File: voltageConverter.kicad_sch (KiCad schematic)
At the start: 5 parts, among them IC1 Voltage Converter (ADP7158ARD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

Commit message: Finished schematic and fully routed PCB.
Signed-off-by: Logan Tolbert <xem6df@virginia.edu>
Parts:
- renumbered C5 to C12, C6 to C13, C7 to C14, C8 to C15
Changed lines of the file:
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@@
 		(dnp no)
 		(fields_autoplaced yes)
-		(property "Reference" "C6"
+		(property "Reference" "C13"
 			(at 121.92 87.6299 0)
 			(effects
@@
 			(project "COMM"
 				(path "/b0bd204d-ca77-4624-acd2-31813bf00a6c/aa984c0d-c4b1-428c-b5e1-c08f8c2d2b92"
-					(reference "C6")
+					(reference "C13")
 					(unit 1)
 				)
@@
 		(dnp no)
 		(fields_autoplaced yes)
-		(property "Reference" "C8"
+		(property "Reference" "C15"
 			(at 190.5 82.5499 0)
 			(effects
@@
 			(project "COMM"
 				(path "/b0bd204d-ca77-4624-acd2-31813bf00a6c/aa984c0d-c4b1-428c-b5e1-c08f8c2d2b92"
-					(reference "C8")
+					(reference "C15")
 					(unit 1)
 				)
@@
 		(dnp no)
 		(fields_autoplaced yes)
-		(property "Reference" "#PWR023"
+		(property "Reference" "#PWR030"
 			(at 152.4 107.95 0)
 			(effects
@@
 			(project "COMM"
 				(path "/b0bd204d-ca77-4624-acd2-31813bf00a6c/aa984c0d-c4b1-428c-b5e1-c08f8c2d2b92"
-					(reference "#PWR023")
+					(reference "#PWR030")
 					(unit 1)
 				)
@@
 		(dnp no)
 		(fields_autoplaced yes)
-		(property "Reference" "#PWR024"
+		(property "Reference" "#PWR031"
 			(at 180.34 107.95 0)
 			(effects
@@
 			(project "COMM"
 				(path "/b0bd204d-ca77-4624-acd2-31813bf00a6c/aa984c0d-c4b1-428c-b5e1-c08f8c2d2b92"
-					(reference "#PWR024")
+					(reference "#PWR031")
 					(unit 1)
 				)
@@
 		(dnp no)
 		(fields_autoplaced yes)
-		(property "Reference" "#PWR025"
+		(property "Reference" "#PWR032"
 			(at 186.69 93.98 0)
 			(effects
@@
 			(project "COMM"
 				(path "/b0bd204d-ca77-4624-acd2-31813bf00a6c/aa984c0d-c4b1-428c-b5e1-c08f8c2d2b92"
-					(reference "#PWR025")
+					(reference "#PWR032")
 					(unit 1)
 				)
@@
 		(dnp no)
 		(fields_autoplaced yes)
-		(property "Reference" "C7"
+		(property "Reference" "C14"
 			(at 184.15 96.5199 0)
 			(effects
@@
 			(project "COMM"
 				(path "/b0bd204d-ca77-4624-acd2-31813bf00a6c/aa984c0d-c4b1-428c-b5e1-c08f8c2d2b92"
-					(reference "C7")
+					(reference "C14")
 					(unit 1)
 				)
@@
 		(dnp no)
 		(fields_autoplaced yes)
-		(property "Reference" "C5"
+		(property "Reference" "C12"
 			(at 107.95 87.6299 0)
 			(effects
@@
 			(project "COMM"
 				(path "/b0bd204d-ca77-4624-acd2-31813bf00a6c/aa984c0d-c4b1-428c-b5e1-c08f8c2d2b92"
-					(reference "C5")
+					(reference "C12")
 					(unit 1)
 				)
@@
 		(dnp no)
 		(fields_autoplaced yes)
-		(property "Reference" "#PWR022"
+		(property "Reference" "#PWR029"
 			(at 118.11 99.06 0)
 			(effects
@@
 			(project "COMM"
 				(path "/b0bd204d-ca77-4624-acd2-31813bf00a6c/aa984c0d-c4b1-428c-b5e1-c08f8c2d2b92"
-					(reference "#PWR022")
+					(reference "#PWR029")
 					(unit 1)
 				)
@@
 		(dnp no)
 		(fields_autoplaced yes)
-		(property "Reference" "#PWR021"
+		(property "Reference" "#PWR028"
 			(at 104.14 99.06 0)
 			(effects
@@
 			(project "COMM"
 				(path "/b0bd204d-ca77-4624-acd2-31813bf00a6c/aa984c0d-c4b1-428c-b5e1-c08f8c2d2b92"
-					(reference "#PWR021")
-					(unit 1)
-				)
+					(reference "#PWR028")
+					(unit 1)
+				)

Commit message: Added pull-up to CS pin on DMR module.
Signed-off-by: Logan Tolbert <xem6df@virginia.edu>
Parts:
- renumbered C12 to C11, C13 to C12, C14 to C13, C15 to C14
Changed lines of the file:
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@@
 		(dnp no)
 		(fields_autoplaced yes)
-		(property "Reference" "C13"
+		(property "Reference" "C12"
 			(at 121.92 87.6299 0)
 			(effects
@@
 			(project "COMM"
 				(path "/b0bd204d-ca77-4624-acd2-31813bf00a6c/aa984c0d-c4b1-428c-b5e1-c08f8c2d2b92"
-					(reference "C13")
+					(reference "C12")
 					(unit 1)
 				)
@@
 		(dnp no)
 		(fields_autoplaced yes)
-		(property "Reference" "C15"
+		(property "Reference" "C14"
 			(at 190.5 82.5499 0)
 			(effects
@@
 			(project "COMM"
 				(path "/b0bd204d-ca77-4624-acd2-31813bf00a6c/aa984c0d-c4b1-428c-b5e1-c08f8c2d2b92"
-					(reference "C15")
+					(reference "C14")
 					(unit 1)
 				)
@@
 		(dnp no)
 		(fields_autoplaced yes)
-		(property "Reference" "#PWR030"
+		(property "Reference" "#PWR029"
 			(at 152.4 107.95 0)
 			(effects
@@
 			(project "COMM"
 				(path "/b0bd204d-ca77-4624-acd2-31813bf00a6c/aa984c0d-c4b1-428c-b5e1-c08f8c2d2b92"
-					(reference "#PWR030")
+					(reference "#PWR029")
 					(unit 1)
 				)
@@
 		(dnp no)
 		(fields_autoplaced yes)
-		(property "Reference" "#PWR031"
+		(property "Reference" "#PWR030"
 			(at 180.34 107.95 0)
 			(effects
@@
 			(project "COMM"
 				(path "/b0bd204d-ca77-4624-acd2-31813bf00a6c/aa984c0d-c4b1-428c-b5e1-c08f8c2d2b92"
-					(reference "#PWR031")
+					(reference "#PWR030")
 					(unit 1)
 				)
@@
 		(dnp no)
 		(fields_autoplaced yes)
-		(property "Reference" "#PWR032"
+		(property "Reference" "#PWR031"
 			(at 186.69 93.98 0)
 			(effects
@@
 			(project "COMM"
 				(path "/b0bd204d-ca77-4624-acd2-31813bf00a6c/aa984c0d-c4b1-428c-b5e1-c08f8c2d2b92"
-					(reference "#PWR032")
+					(reference "#PWR031")
 					(unit 1)
 				)
@@
 		(dnp no)
 		(fields_autoplaced yes)
-		(property "Reference" "C14"
+		(property "Reference" "C13"
 			(at 184.15 96.5199 0)
 			(effects
@@
 			(project "COMM"
 				(path "/b0bd204d-ca77-4624-acd2-31813bf00a6c/aa984c0d-c4b1-428c-b5e1-c08f8c2d2b92"
-					(reference "C14")
+					(reference "C13")
 					(unit 1)
 				)
@@
 		(dnp no)
 		(fields_autoplaced yes)
-		(property "Reference" "C12"
+		(property "Reference" "C11"
 			(at 107.95 87.6299 0)
 			(effects
@@
 			(project "COMM"
 				(path "/b0bd204d-ca77-4624-acd2-31813bf00a6c/aa984c0d-c4b1-428c-b5e1-c08f8c2d2b92"
-					(reference "C12")
+					(reference "C11")
 					(unit 1)
 				)
@@
 		(dnp no)
 		(fields_autoplaced yes)
-		(property "Reference" "#PWR029"
+		(property "Reference" "#PWR028"
 			(at 118.11 99.06 0)
 			(effects
@@
 			(project "COMM"
 				(path "/b0bd204d-ca77-4624-acd2-31813bf00a6c/aa984c0d-c4b1-428c-b5e1-c08f8c2d2b92"
-					(reference "#PWR029")
+					(reference "#PWR028")
 					(unit 1)
 				)
@@
 		(dnp no)
 		(fields_autoplaced yes)
-		(property "Reference" "#PWR028"
+		(property "Reference" "#PWR027"
 			(at 104.14 99.06 0)
 			(effects
@@
 			(project "COMM"
 				(path "/b0bd204d-ca77-4624-acd2-31813bf00a6c/aa984c0d-c4b1-428c-b5e1-c08f8c2d2b92"
-					(reference "#PWR028")
-					(unit 1)
-				)
+					(reference "#PWR027")
+					(unit 1)
+				)

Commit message: Addressed most comments from McPherson, modified schematic.
Signed-off-by: Logan Tolbert <xem6df@virginia.edu>
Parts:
- added C21: 10 μF, C_10uF:CAPC1005X70N, symbol Device:C
- renumbered C11 to C17, C12 to C18, C13 to C19, C14 to C20
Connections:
- net GND: now also C21.2
- net VIN: now also C21.1
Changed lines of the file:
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@@
+	)
+	(junction
+		(at 196.85 109.22)
+		(diameter 0)
+		(color 0 0 0 0)
 	)
 	(junction
@@
 		(pts
 			(xy 180.34 85.09) (xy 180.34 93.98)
+		)
+		(stroke
+			(width 0)
+			(type default)
+		)
+	)
+	(wire
+		(pts
+			(xy 196.85 110.49) (xy 196.85 109.22)
 		)
 		(stroke
@@
 		(dnp no)
 		(fields_autoplaced yes)
-		(property "Reference" "C12"
+		(property "Reference" "C18"
 			(at 121.92 87.6299 0)
 			(effects
@@
 			(project "COMM"
 				(path "/b0bd204d-ca77-4624-acd2-31813bf00a6c/aa984c0d-c4b1-428c-b5e1-c08f8c2d2b92"
-					(reference "C12")
+					(reference "C18")
 					(unit 1)
 				)
@@
 		(dnp no)
 		(fields_autoplaced yes)
-		(property "Reference" "C14"
+		(property "Reference" "C20"
 			(at 190.5 82.5499 0)
 			(effects
@@
 			(project "COMM"
 				(path "/b0bd204d-ca77-4624-acd2-31813bf00a6c/aa984c0d-c4b1-428c-b5e1-c08f8c2d2b92"
-					(reference "C14")
+					(reference "C20")
 					(unit 1)
 				)
@@
 		(dnp no)
 		(fields_autoplaced yes)
-		(property "Reference" "#PWR029"
+		(property "Reference" "#PWR041"
 			(at 152.4 107.95 0)
 			(effects
@@
 			(project "COMM"
 				(path "/b0bd204d-ca77-4624-acd2-31813bf00a6c/aa984c0d-c4b1-428c-b5e1-c08f8c2d2b92"
-					(reference "#PWR029")
+					(reference "#PWR041")
 					(unit 1)
 				)
@@
 		(dnp no)
 		(fields_autoplaced yes)
-		(property "Reference" "#PWR030"
+		(property "Reference" "#PWR042"
 			(at 180.34 107.95 0)
 			(effects
@@
 			(project "COMM"
 				(path "/b0bd204d-ca77-4624-acd2-31813bf00a6c/aa984c0d-c4b1-428c-b5e1-c08f8c2d2b92"
-					(reference "#PWR030")
+					(reference "#PWR042")
 					(unit 1)
 				)
@@
 		(dnp no)
 		(fields_autoplaced yes)
-		(property "Reference" "#PWR031"
+		(property "Reference" "#PWR043"
 			(at 186.69 93.98 0)
 			(effects
@@
 			(project "COMM"
 				(path "/b0bd204d-ca77-4624-acd2-31813bf00a6c/aa984c0d-c4b1-428c-b5e1-c08f8c2d2b92"
-					(reference "#PWR031")
+					(reference "#PWR043")
 					(unit 1)
 				)
@@
 		(dnp no)
 		(fields_autoplaced yes)
-		(property "Reference" "C13"
+		(property "Reference" "C19"
 			(at 184.15 96.5199 0)
 			(effects
@@
 			(project "COMM"
 				(path "/b0bd204d-ca77-4624-acd2-31813bf00a6c/aa984c0d-c4b1-428c-b5e1-c08f8c2d2b92"
-					(reference "C13")
+					(reference "C19")
 					(unit 1)
 				)
@@
 		(dnp no)
 		(fields_autoplaced yes)
-		(property "Reference" "C11"
+		(property "Reference" "C17"
 			(at 107.95 87.6299 0)
 			(effects
@@
 			(project "COMM"
 				(path "/b0bd204d-ca77-4624-acd2-31813bf00a6c/aa984c0d-c4b1-428c-b5e1-c08f8c2d2b92"
-					(reference "C11")
+					(reference "C17")
 					(unit 1)
 				)
@@
 	(symbol
 		(lib_id "power:GND")
+		(at 196.85 118.11 0)
+		(unit 1)
+		(exclude_from_sim no)
+		(in_bom yes)
+		(on_board yes)
+		(dnp no)
+		(fields_autoplaced yes)
+		(property "Reference" "#PWR044"
+			(at 196.85 124.46 0)
+			(effects
+				(font
+					(size 1.27 1.27)
+				)
+				(hide yes)
+			)
+		)
+		(property "Value" "GND"
+			(at 196.85 123.19 0)
+			(effects
+				(font
+					(size 1.27 1.27)
+				)
+			)
+		)
+		(property "Footprint" ""
+			(at 196.85 118.11 0)
+			(effects
+				(font
+					(size 1.27 1.27)
+				)
+				(hide yes)
+			)
+		)
+		(property "Datasheet" ""
+			(at 196.85 118.11 0)
+			(effects
+				(font
+					(size 1.27 1.27)
+				)
+				(hide yes)
+			)
+		)
+		(property "Description" "Power symbol creates a global label with name \"GND\" , ground"
+			(at 196.85 118.11 0)
+			(effects
+				(font
+					(size 1.27 1.27)
+				)
+				(hide yes)
+			)
+		)
+		(pin "1"
+		)
+		(instances
+			(project "COMM"
+				(path "/b0bd204d-ca77-4624-acd2-31813bf00a6c/aa984c0d-c4b1-428c-b5e1-c08f8c2d2b92"
+					(reference "#PWR044")
+					(unit 1)
+				)
+			)
+		)
+	)
+	(symbol
+		(lib_id "Device:C")
+		(at 196.85 114.3 0)
+		(unit 1)
+		(exclude_from_sim no)
+		(in_bom yes)
+		(on_board yes)
+		(dnp no)
+		(fields_autoplaced yes)
+		(property "Reference" "C21"
+			(at 200.66 113.0299 0)
+			(effects
+				(font
+					(size 1.27 1.27)
+				)
+				(justify left)
+			)
+		)
+		(property "Value" "10 μF"
+			(at 200.66 115.5699 0)
+			(effects
+				(font
+					(size 1.27 1.27)
+				)
+				(justify left)
+			)
+		)
+		(property "Footprint" "C_10uF:CAPC1005X70N"
+			(at 197.8152 118.11 0)
+			(effects
+				(font
+					(size 1.27 1.27)
+				)
+				(hide yes)
+			)
+		)
+		(property "Datasheet" "~"
+			(at 196.85 114.3 0)
+			(effects
+				(font
+					(size 1.27 1.27)
+				)
+				(hide yes)
+			)
+		)
+		(property "Description" "Unpolarized capacitor"
+			(at 196.85 114.3 0)
+			(effects
+				(font
+					(size 1.27 1.27)
+				)
+				(hide yes)
+			)
+		)
+		(pin "2"
+		)
+		(pin "1"
+		)
+		(instances
+			(project "COMM"
+				(path "/b0bd204d-ca77-4624-acd2-31813bf00a6c/aa984c0d-c4b1-428c-b5e1-c08f8c2d2b92"
+					(reference "C21")
+					(unit 1)
+				)
+			)
+		)
+	)
+	(symbol
+		(lib_id "power:GND")
 		(at 118.11 92.71 0)
 		(unit 1)
@@
 		(dnp no)
 		(fields_autoplaced yes)
-		(property "Reference" "#PWR028"
+		(property "Reference" "#PWR040"
 			(at 118.11 99.06 0)
 			(effects
@@
 			(project "COMM"
 				(path "/b0bd204d-ca77-4624-acd2-31813bf00a6c/aa984c0d-c4b1-428c-b5e1-c08f8c2d2b92"
-					(reference "#PWR028")
+					(reference "#PWR040")
 					(unit 1)
 				)
@@
 		(dnp no)
 		(fields_autoplaced yes)
-		(property "Reference" "#PWR027"
+		(property "Reference" "#PWR039"
 			(at 104.14 99.06 0)
 			(effects
@@
 			(project "COMM"
 				(path "/b0bd204d-ca77-4624-acd2-31813bf00a6c/aa984c0d-c4b1-428c-b5e1-c08f8c2d2b92"
-					(reference "#PWR027")
+					(reference "#PWR039")
 					(unit 1)
 				)

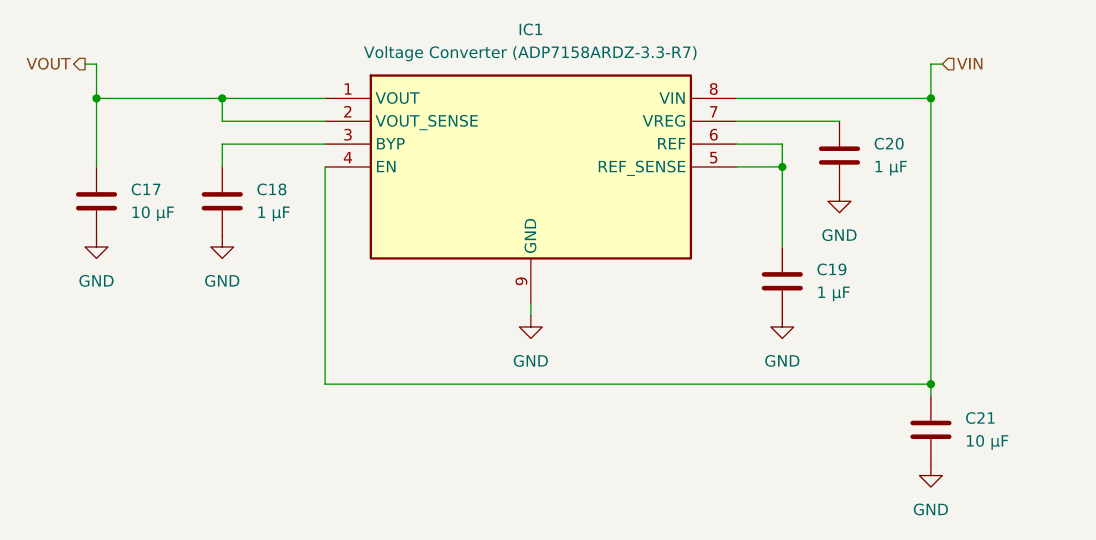
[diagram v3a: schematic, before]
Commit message: Finalized board design, updated DMR module to DMR818S-5W exact dimensions, rerouted PCB according to McPherson's comments. Added TLV61047 5V to 8V booster module.
Signed-off-by: Logan Tolbert <xem6df@virginia.edu>
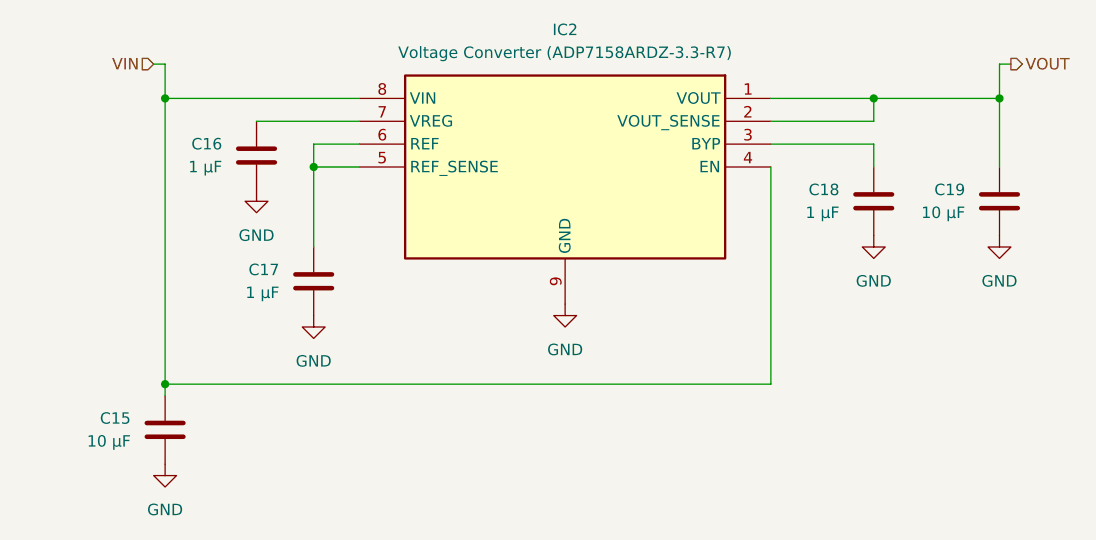
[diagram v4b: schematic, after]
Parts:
- renumbered C21 to C15, C20 to C16, C19 to C17, C17 to C19, IC1 to IC2
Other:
- moved on the sheet: C15, C16, C17, C18, C19, IC2

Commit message: Final COMM board design as of Feb 12 2026, ready to order.
Signed-off-by: Logan Tolbert <xem6df@virginia.edu>
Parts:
- renumbered C15 to C12, C16 to C13, C17 to C14, C18 to C15, C19 to C16
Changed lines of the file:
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@@
 		(dnp no)
 		(fields_autoplaced yes)
-		(property "Reference" "C18"
+		(property "Reference" "C15"
 			(at 186.69 87.6299 0)
 			(effects
@@
 			(project "COMM"
 				(path "/b0bd204d-ca77-4624-acd2-31813bf00a6c/aa984c0d-c4b1-428c-b5e1-c08f8c2d2b92"
-					(reference "C18")
+					(reference "C15")
 					(unit 1)
 				)
@@
 		(dnp no)
 		(fields_autoplaced yes)
-		(property "Reference" "C16"
+		(property "Reference" "C13"
 			(at 118.11 82.5499 0)
 			(effects
@@
 			(project "COMM"
 				(path "/b0bd204d-ca77-4624-acd2-31813bf00a6c/aa984c0d-c4b1-428c-b5e1-c08f8c2d2b92"
-					(reference "C16")
+					(reference "C13")
 					(unit 1)
 				)
@@
 		(dnp no)
 		(fields_autoplaced yes)
-		(property "Reference" "#PWR040"
+		(property "Reference" "#PWR038"
 			(at 156.21 106.68 0)
 			(effects
@@
 			(project "COMM"
 				(path "/b0bd204d-ca77-4624-acd2-31813bf00a6c/aa984c0d-c4b1-428c-b5e1-c08f8c2d2b92"
-					(reference "#PWR040")
+					(reference "#PWR038")
 					(unit 1)
 				)
@@
 		(dnp no)
 		(fields_autoplaced yes)
-		(property "Reference" "#PWR039"
+		(property "Reference" "#PWR037"
 			(at 128.27 107.95 0)
 			(effects
@@
 			(project "COMM"
 				(path "/b0bd204d-ca77-4624-acd2-31813bf00a6c/aa984c0d-c4b1-428c-b5e1-c08f8c2d2b92"
-					(reference "#PWR039")
+					(reference "#PWR037")
 					(unit 1)
 				)
@@
 		(dnp no)
 		(fields_autoplaced yes)
-		(property "Reference" "#PWR038"
+		(property "Reference" "#PWR036"
 			(at 121.92 93.98 0)
 			(effects
@@
 			(project "COMM"
 				(path "/b0bd204d-ca77-4624-acd2-31813bf00a6c/aa984c0d-c4b1-428c-b5e1-c08f8c2d2b92"
-					(reference "#PWR038")
+					(reference "#PWR036")
 					(unit 1)
 				)
@@
 		(dnp no)
 		(fields_autoplaced yes)
-		(property "Reference" "C17"
+		(property "Reference" "C14"
 			(at 124.46 96.5199 0)
 			(effects
@@
 			(project "COMM"
 				(path "/b0bd204d-ca77-4624-acd2-31813bf00a6c/aa984c0d-c4b1-428c-b5e1-c08f8c2d2b92"
-					(reference "C17")
+					(reference "C14")
 					(unit 1)
 				)
@@
 		(dnp no)
 		(fields_autoplaced yes)
-		(property "Reference" "C19"
+		(property "Reference" "C16"
 			(at 200.66 87.6299 0)
 			(effects
@@
 			(project "COMM"
 				(path "/b0bd204d-ca77-4624-acd2-31813bf00a6c/aa984c0d-c4b1-428c-b5e1-c08f8c2d2b92"
-					(reference "C19")
+					(reference "C16")
 					(unit 1)
 				)
@@
 		(dnp no)
 		(fields_autoplaced yes)
-		(property "Reference" "#PWR037"
+		(property "Reference" "#PWR035"
 			(at 111.76 124.46 0)
 			(effects
@@
 			(project "COMM"
 				(path "/b0bd204d-ca77-4624-acd2-31813bf00a6c/aa984c0d-c4b1-428c-b5e1-c08f8c2d2b92"
-					(reference "#PWR037")
+					(reference "#PWR035")
 					(unit 1)
 				)
@@
 		(dnp no)
 		(fields_autoplaced yes)
-		(property "Reference" "C15"
+		(property "Reference" "C12"
 			(at 107.95 113.0299 0)
 			(effects
@@
 			(project "COMM"
 				(path "/b0bd204d-ca77-4624-acd2-31813bf00a6c/aa984c0d-c4b1-428c-b5e1-c08f8c2d2b92"
-					(reference "C15")
+					(reference "C12")
 					(unit 1)
 				)
@@
 		(dnp no)
 		(fields_autoplaced yes)
-		(property "Reference" "#PWR041"
+		(property "Reference" "#PWR039"
 			(at 190.5 99.06 0)
 			(effects
@@
 			(project "COMM"
 				(path "/b0bd204d-ca77-4624-acd2-31813bf00a6c/aa984c0d-c4b1-428c-b5e1-c08f8c2d2b92"
-					(reference "#PWR041")
+					(reference "#PWR039")
 					(unit 1)
 				)
@@
 		(dnp no)
 		(fields_autoplaced yes)
-		(property "Reference" "#PWR042"
+		(property "Reference" "#PWR040"
 			(at 204.47 99.06 0)
 			(effects
@@
 			(project "COMM"
 				(path "/b0bd204d-ca77-4624-acd2-31813bf00a6c/aa984c0d-c4b1-428c-b5e1-c08f8c2d2b92"
-					(reference "#PWR042")
-					(unit 1)
-				)
+					(reference "#PWR040")
+					(unit 1)
+				)
